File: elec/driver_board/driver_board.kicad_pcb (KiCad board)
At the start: 2 copper layers, 226.2 x 90.5 mm, 123 parts, among them J1 rotary_encoder, J10 Conn motor 0, J11 Conn motor 1, J12 Conn motor 0, J13 Conn motor 1, J14 Conn motor 0, J15 Conn motor 1, J16 Conn motor 0, J17 Conn motor 1, J18 Conn motor 0, J19 Conn motor 1, J2 DCF77 board, J20 Conn motor 0, J21 Conn motor 1, J22 Conn motor 0, J23 Conn motor 1, J24 Conn motor 0, J25 Conn motor 1, J26 Conn motor 0, J27 Conn motor 1, J3 RTC, J4 Conn motor 0, J5 Conn motor 1, J6 Conn motor 0, J7 Conn motor 1, J8 Conn motor 0, J9 Conn motor 1, U1 ESP32-C3-DEVKITM-1, U11 74HCT595, U13 74HCT595, U15 74HCT595, U17 74HCT595, U19 74HCT595, U2 TXB0102DCT, U21 74HCT595, U23 74HCT595, U25 74HCT595, U3 74HCT595, U5 74HCT595, U7 74HCT595, U9 74HCT595

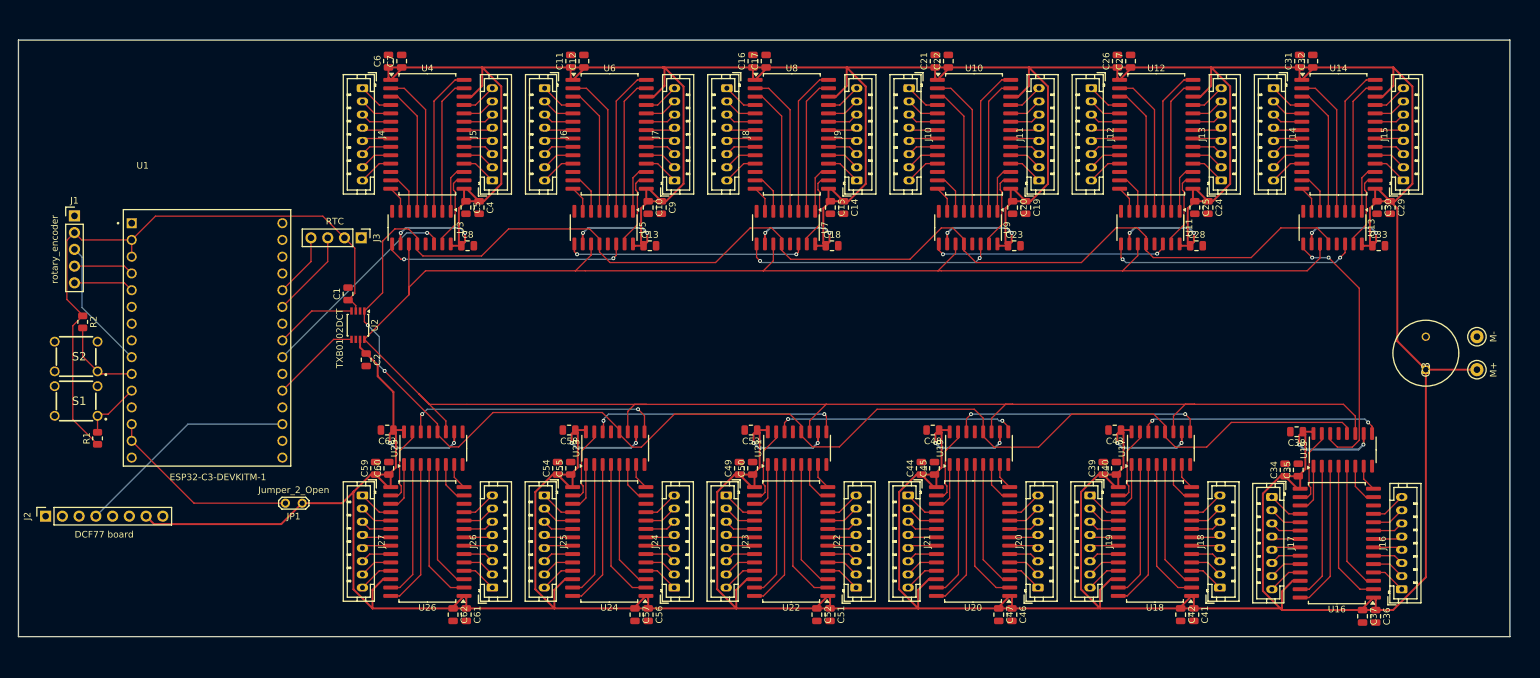
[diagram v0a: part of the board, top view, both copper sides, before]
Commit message: PCB done, ready to be ordered
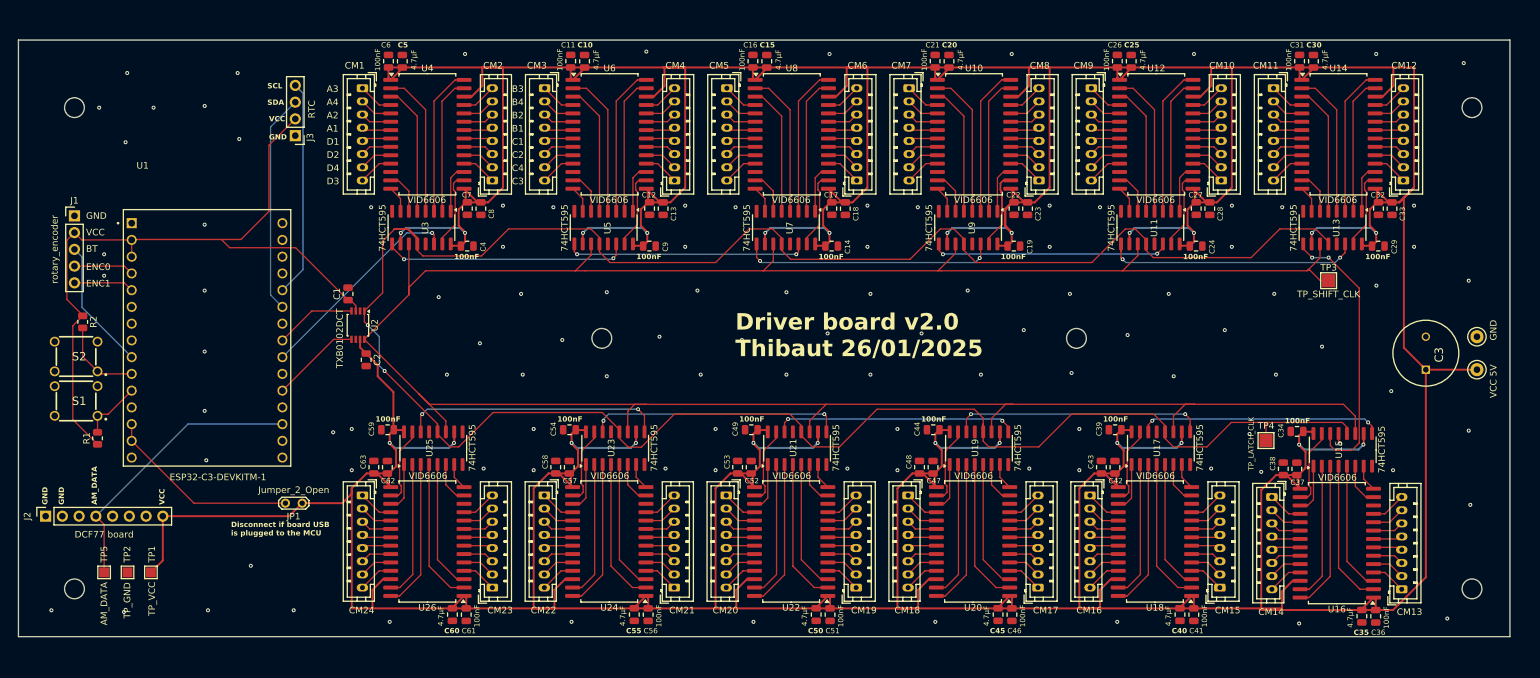
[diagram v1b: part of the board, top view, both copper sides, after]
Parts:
- added TP1: TP_VCC, TestPoint:TestPoint_Pad_1.5x1.5mm, F.Cu at (61.6, 120.5)
- added TP2: TP_GND, TestPoint:TestPoint_Pad_1.5x1.5mm, F.Cu at (58.0, 120.5)
- added TP3: TP_SHIFT_CLK, TestPoint:TestPoint_Pad_2.0x2.0mm, F.Cu at (240.2, 76.2)
- added TP4: TP_LATCH_CLK, TestPoint:TestPoint_Pad_2.0x2.0mm, F.Cu at (230.8, 100.5)
- added TP5: AM_DATA, TestPoint:TestPoint_Pad_1.5x1.5mm, F.Cu at (54.5, 120.5)
- GND_DCDC1: value M- -> GND
- U10, U12, U14, U16, U18, U20, U22, U24, U26, U4, U6, U8: value ~ -> VID6606
- VCC_DCDC1: value M+ -> VCC 5V
- moved C17 24.5 mm to (164.9, 65.3), turned to -90 degrees
- moved C22 24.5 mm to (192.5, 65.3), turned to -90 degrees
- moved C27 24.5 mm to (220.2, 65.3), turned to -90 degrees
- moved C32 24.5 mm to (247.8, 65.3), turned to -90 degrees
- moved C7 24.5 mm to (109.6, 65.3), turned to -90 degrees
- moved C12 24.5 mm to (137.2, 65.3), turned to -90 degrees
- moved C37 24.5 mm to (235.4, 104.8), turned to 90 degrees
- moved C42 24.5 mm to (207.8, 104.6), turned to 90 degrees
- moved C52 24.5 mm to (152.7, 104.6), turned to 90 degrees
- moved C62 24.5 mm to (97.5, 104.6), turned to 90 degrees
- moved C57 24.5 mm to (125.1, 104.6), turned to 90 degrees
- moved C47 24.5 mm to (180.2, 104.6), turned to 90 degrees
- moved C55 24.2 mm to (134.9, 126.9), turned to -90 degrees
- moved C35 24.2 mm to (245.3, 127.1), turned to -90 degrees
- moved C40 24.2 mm to (217.7, 126.9), turned to -90 degrees
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- renumbered J4 to CM1, J13 to CM10, J14 to CM11, J15 to CM12, J16 to CM13, J17 to CM14, J18 to CM15, J19 to CM16, J20 to CM17, J21 to CM18, J22 to CM19, J5 to CM2, J23 to CM20, J24 to CM21, J25 to CM22, J26 to CM23, J27 to CM24, J6 to CM3, J7 to CM4, J8 to CM5, J9 to CM6, J10 to CM7, J11 to CM8, J12 to CM9
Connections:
- J2 pad 7: VCC -> unconnected-(J2-Pin_7-Pad7)
- J2 pad 8: unconnected-(J2-Pin_8-Pad8) -> VCC
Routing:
- net VCC: track 1206.4 -> 1230.6 mm
- net /control_board/SCL_RTC: track 9.74 -> 32.8 mm
- net /control_board/SDA_RTC: track 13.3 -> 33.4 mm
- net /control_board/VCC_3V3: track 95.4 -> 111.1 mm
- net LATCH_CLOCK: track 371.0 -> 380.6 mm
- net /control_board/AM_DATA: track 34.1 -> 43.1 mm
- net /motor_driver3/DIR_D: track 11.9 -> 18.8 mm
- net /motor_driver3/DATA_OUT: track 37.2 -> 34.7 mm
- net GND: track 0.00 -> 1.65 mm, vias 0 -> 107
- net /motor_driver7/DATA_OUT: track 38.5 -> 39.6 mm
- net /motor_driver4/DATA_OUT: track 38.3 -> 39.5 mm
- net /motor_driver2/DATA_OUT: track 38.7 -> 39.8 mm
- net SHIFT_CLOCK: track 372.7 -> 373.6 mm
- net /motor_driver8/DATA_OUT: track 36.8 -> 36.0 mm
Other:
- outline, holes or cut-outs redrawn
- board text added: "A1"
- board text added: "A2"
- board text added: "A3"
- board text added: "A4"
- board text added: "AM_DATA"
- board text added: "B1"
- board text added: "B2"
- board text added: "B3"
- board text added: "B4"
- board text added: "BT"
- board text added: "C1"
- board text added: "C2"
- board text added: "C3"
- board text added: "C4"
- board text added: "D1"
- board text added: "D2"
- board text added: "D3"
- board text added: "D4"
- board text added: "Disconnect if board USB is plugged to the MCU"
- board text added: "Driver board v2.0 Thibaut 26/01/2025"
- board text added: "ENC0"
- board text added: "ENC1"
- board text added: "GND"
- board text added: "SCL"
- board text added: "SDA"
- board text added: "VCC"

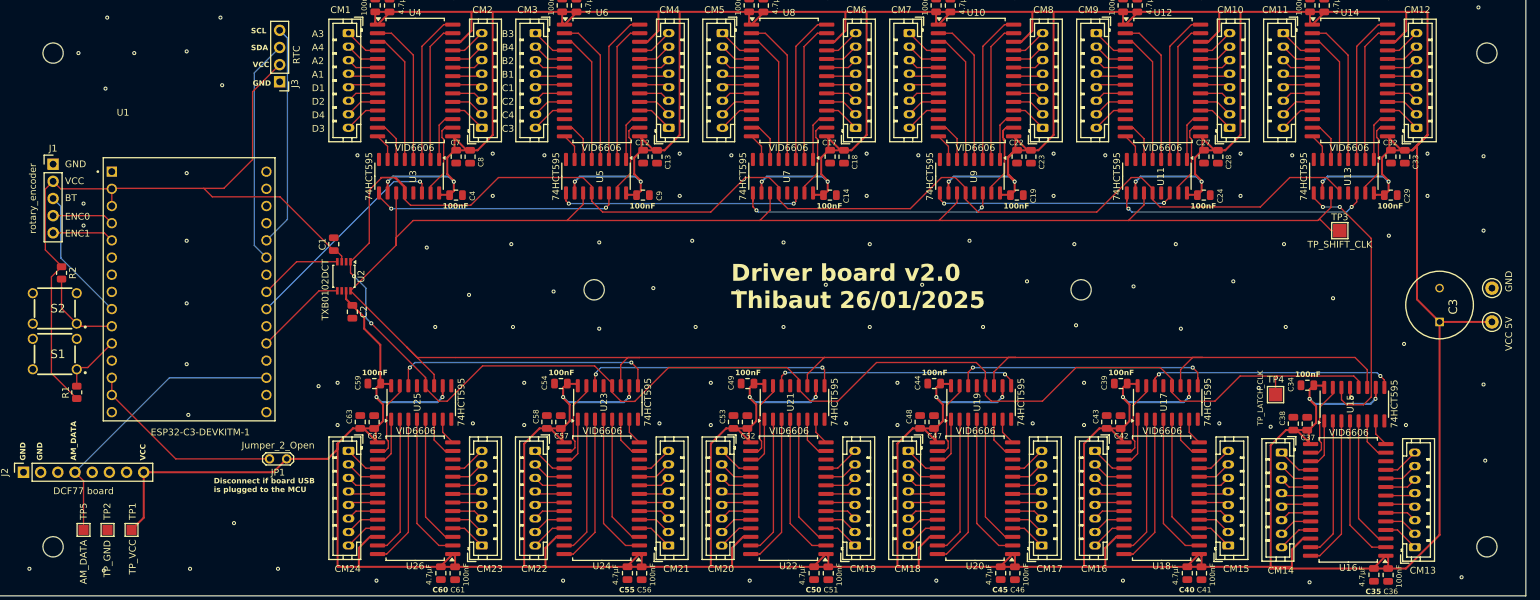
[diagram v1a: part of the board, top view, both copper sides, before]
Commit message: Update footprint of the level shifter
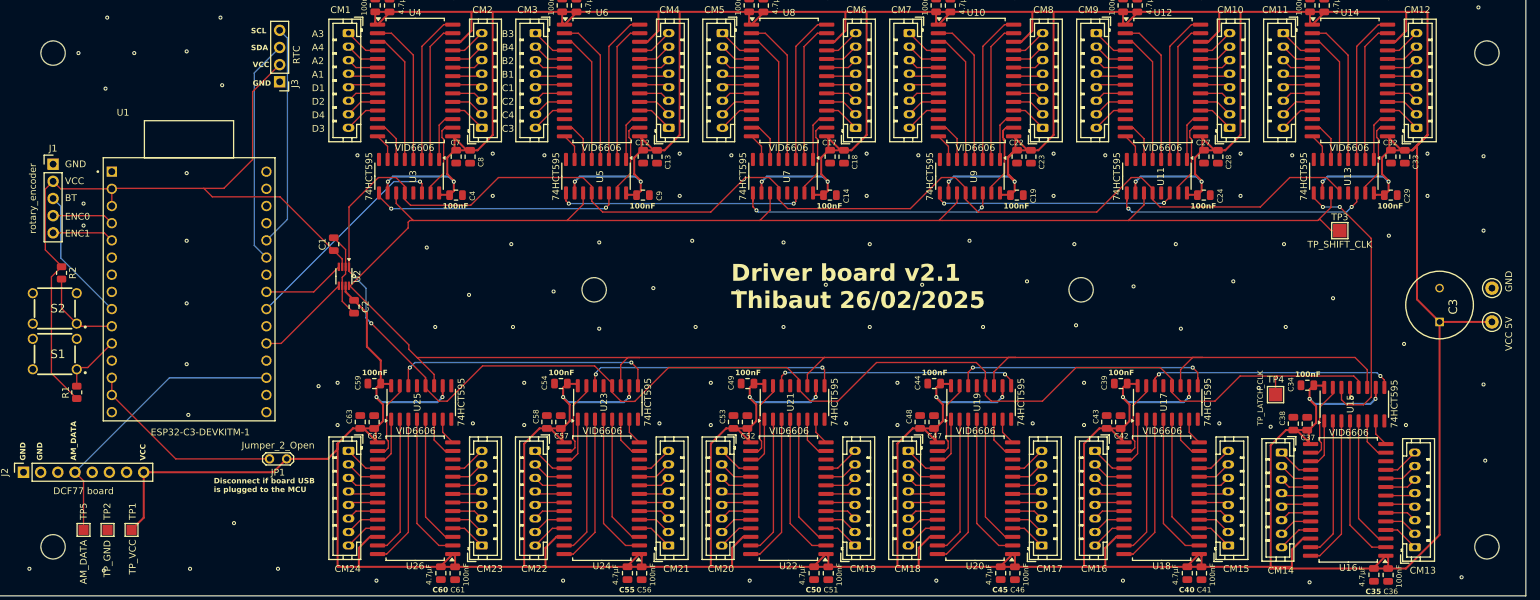
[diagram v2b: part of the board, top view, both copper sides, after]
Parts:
- U2: footprint Package_SO:TSSOP-8_3x3mm_P0.65mm -> Package_SO:VSSOP-8_2.3x2mm_P0.5mm
- moved C2 0.79 mm to (94.5, 87.5)
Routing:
- net GND: track 1.65 -> 14.5 mm
- net LATCH_CLOCK: track 380.6 -> 376.2 mm
- net SHIFT_CLOCK: track 373.6 -> 369.5 mm
- net VCC: track 1230.6 -> 1231.4 mm
- net /control_board/VCC_3V3: track 111.1 -> 111.7 mm
- net /control_board/SHIFT_CLOCK_3V3: track 13.7 -> 14.2 mm
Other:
- outline, holes or cut-outs redrawn
- board text added: "Driver board v2.1 Thibaut 26/02/2025"
- board text removed: "Driver board v2.0 Thibaut 26/01/2025"

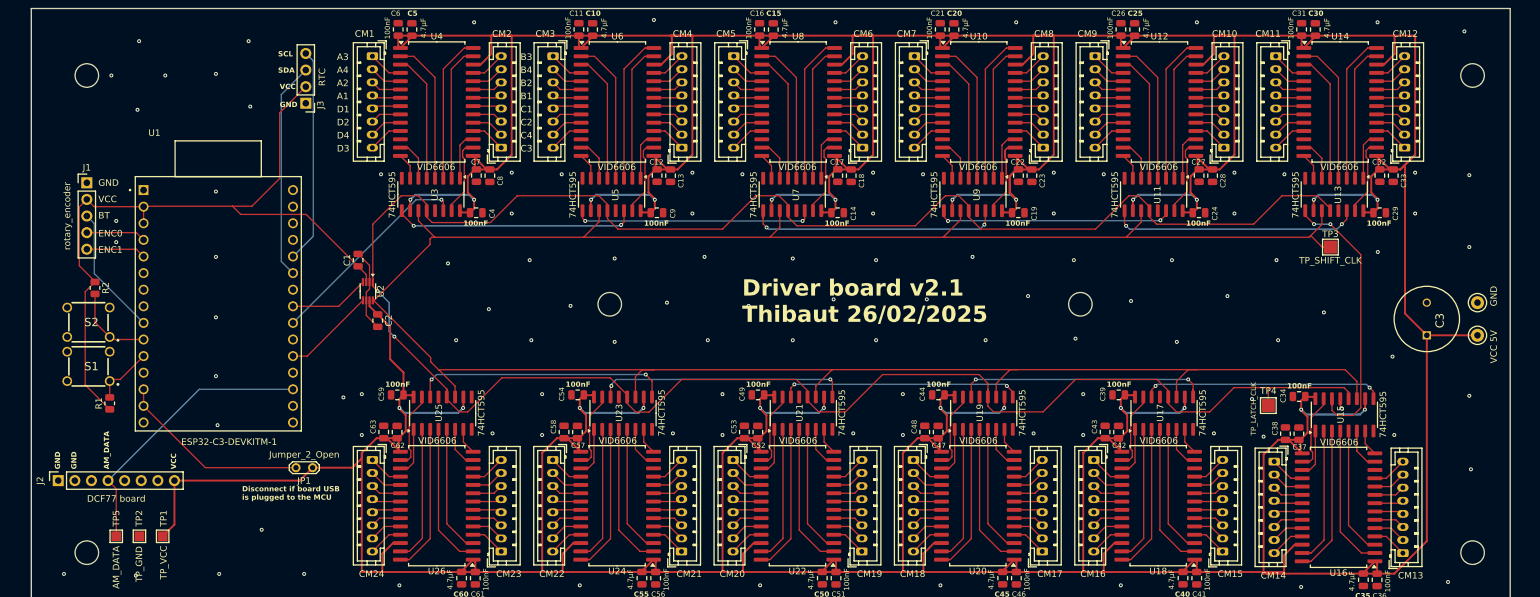
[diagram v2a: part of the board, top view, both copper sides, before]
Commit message: Various updates
Reposition rotary encoder
reposition RTC
add GND pads
update footprint of the big capa
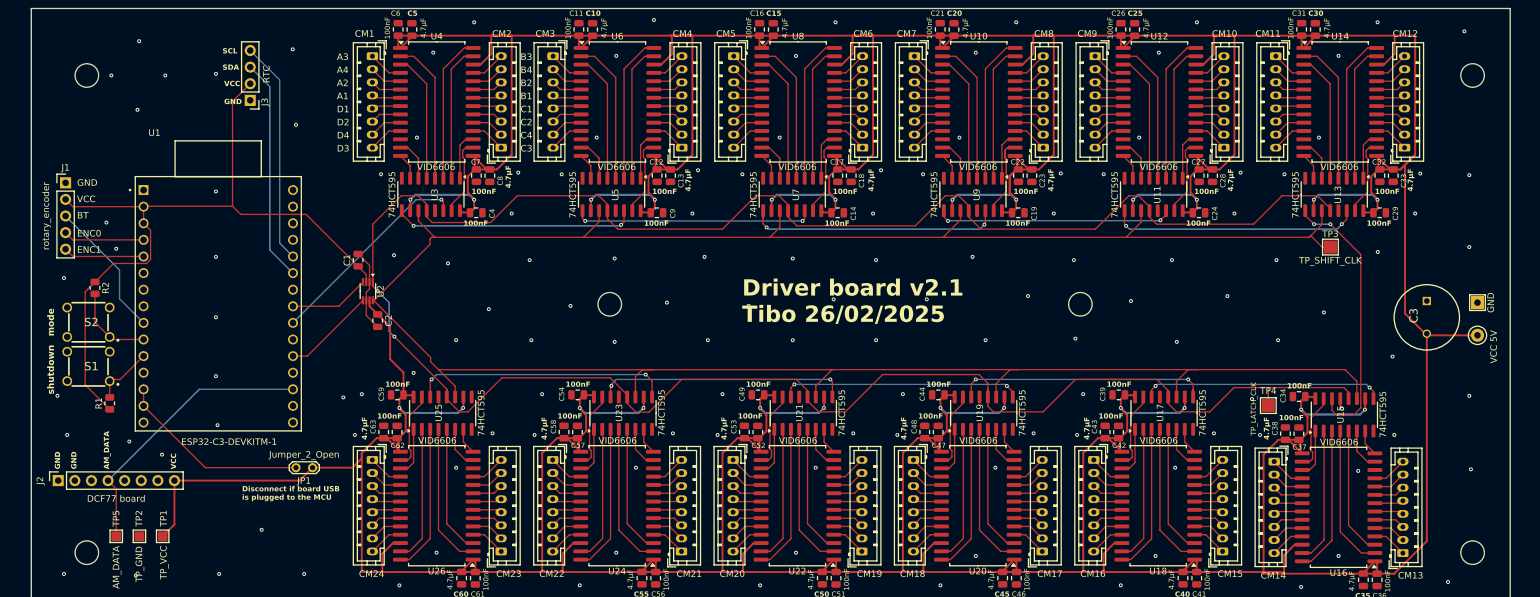
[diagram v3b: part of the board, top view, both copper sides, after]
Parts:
- GND_DCDC1: footprint TestPoint:TestPoint_Keystone_5000-5004_Miniature -> TestPoint:TestPoint_THTPad_2.0x2.0mm_Drill1.0mm
- S1: value Button shutdown -> shutdown
- S2: value Button mode -> mode
- moved J3 8.51 mm to (75.0, 53.8)
- moved C3 5.25 mm to (255.0, 84.5), turned to -90 degrees
- moved J1 3.25 mm to (46.8, 66.4)
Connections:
- C3 pad 1: VCC -> GND
- C3 pad 2: GND -> VCC
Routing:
- net /control_board/PIN_ENCODER_1: track 9.14 -> 12.4 mm
- net /control_board/PIN_ENCODER_0: track 9.14 -> 12.4 mm
- net /control_board/SCL_RTC: track 32.8 -> 34.2 mm
- net /control_board/PIN_BUTTON_ENCODER: track 19.9 -> 21.3 mm
- net /control_board/SDA_RTC: track 33.4 -> 34.2 mm
- net GND: vias 107 -> 138
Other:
- board text added: "Driver board v2.1 Tibo 26/02/2025"
- board text removed: "Driver board v2.1 Thibaut 26/02/2025"

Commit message: Update silkscreen
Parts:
- removed CM1, CM11, CM13, CM15, CM17, CM19, CM21, CM23, CM3, CM5, CM7, CM9: Conn motor 0, Connector_JST:JST_PH_B8B-PH-K_1x08_P2.00mm_Vertical
- removed CM10, CM12, CM14, CM16, CM18, CM2, CM20, CM22, CM24, CM4, CM6, CM8: Conn motor 1, Connector_JST:JST_PH_B8B-PH-K_1x08_P2.00mm_Vertical
- added M1: Conn motor 0, Connector_JST:JST_PH_B8B-PH-K_1x08_P2.00mm_Vertical, F.Cu at (93.7, 47.0)
- added M10: Conn motor 1, Connector_JST:JST_PH_B8B-PH-K_1x08_P2.00mm_Vertical, F.Cu at (224.0, 61.0)
- added M11: Conn motor 0, Connector_JST:JST_PH_B8B-PH-K_1x08_P2.00mm_Vertical, F.Cu at (231.9, 47.0)
- added M12: Conn motor 1, Connector_JST:JST_PH_B8B-PH-K_1x08_P2.00mm_Vertical, F.Cu at (251.6, 61.0)
- added M13: Conn motor 0, Connector_JST:JST_PH_B8B-PH-K_1x08_P2.00mm_Vertical, F.Cu at (251.3, 123.1)
- added M14: Conn motor 1, Connector_JST:JST_PH_B8B-PH-K_1x08_P2.00mm_Vertical, F.Cu at (231.6, 109.1)
- added M15: Conn motor 0, Connector_JST:JST_PH_B8B-PH-K_1x08_P2.00mm_Vertical, F.Cu at (223.8, 122.8)
- added M16: Conn motor 1, Connector_JST:JST_PH_B8B-PH-K_1x08_P2.00mm_Vertical, F.Cu at (204.1, 108.8)
- added M17: Conn motor 0, Connector_JST:JST_PH_B8B-PH-K_1x08_P2.00mm_Vertical, F.Cu at (196.2, 122.8)
- added M18: Conn motor 1, Connector_JST:JST_PH_B8B-PH-K_1x08_P2.00mm_Vertical, F.Cu at (176.5, 108.8)
- added M19: Conn motor 0, Connector_JST:JST_PH_B8B-PH-K_1x08_P2.00mm_Vertical, F.Cu at (168.6, 122.8)
- added M2: Conn motor 1, Connector_JST:JST_PH_B8B-PH-K_1x08_P2.00mm_Vertical, F.Cu at (113.4, 61.0)
- added M20: Conn motor 1, Connector_JST:JST_PH_B8B-PH-K_1x08_P2.00mm_Vertical, F.Cu at (148.9, 108.8)
- added M21: Conn motor 0, Connector_JST:JST_PH_B8B-PH-K_1x08_P2.00mm_Vertical, F.Cu at (141.0, 122.8)
- added M22: Conn motor 1, Connector_JST:JST_PH_B8B-PH-K_1x08_P2.00mm_Vertical, F.Cu at (121.3, 108.8)
- added M23: Conn motor 0, Connector_JST:JST_PH_B8B-PH-K_1x08_P2.00mm_Vertical, F.Cu at (113.4, 122.8)
- added M24: Conn motor 1, Connector_JST:JST_PH_B8B-PH-K_1x08_P2.00mm_Vertical, F.Cu at (93.7, 108.8)
- added M3: Conn motor 0, Connector_JST:JST_PH_B8B-PH-K_1x08_P2.00mm_Vertical, F.Cu at (121.3, 47.0)
- added M4: Conn motor 1, Connector_JST:JST_PH_B8B-PH-K_1x08_P2.00mm_Vertical, F.Cu at (141.0, 61.0)
- added M5: Conn motor 0, Connector_JST:JST_PH_B8B-PH-K_1x08_P2.00mm_Vertical, F.Cu at (149.0, 47.0)
- added M6: Conn motor 1, Connector_JST:JST_PH_B8B-PH-K_1x08_P2.00mm_Vertical, F.Cu at (168.7, 61.0)
- added M7: Conn motor 0, Connector_JST:JST_PH_B8B-PH-K_1x08_P2.00mm_Vertical, F.Cu at (176.6, 47.0)
- added M8: Conn motor 1, Connector_JST:JST_PH_B8B-PH-K_1x08_P2.00mm_Vertical, F.Cu at (196.3, 61.0)
- added M9: Conn motor 0, Connector_JST:JST_PH_B8B-PH-K_1x08_P2.00mm_Vertical, F.Cu at (204.3, 47.0)
- S1: value shutdown -> Button shutdown
- S2: value mode -> Button mode
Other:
- board text added: "DATA_OUT"
- board text added: "Disconnect if USB is plugged to the ESP32"
- board text added: "Driver board v2.1 Thibaut 26/02/2025"
- board text added: "LATCH"
- board text added: "SCL_RTC"
- board text added: "SDA_RTC"
- board text added: "SHIFT_CLK"
- board text removed: "Disconnect if board USB is plugged to the MCU"
- board text removed: "Driver board v2.1 Tibo 26/02/2025"

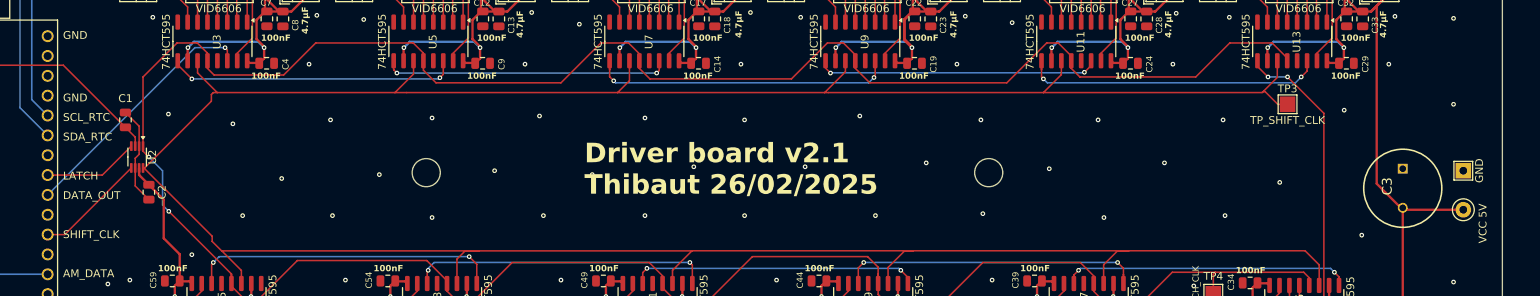
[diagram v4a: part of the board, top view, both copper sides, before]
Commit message: Update symbols
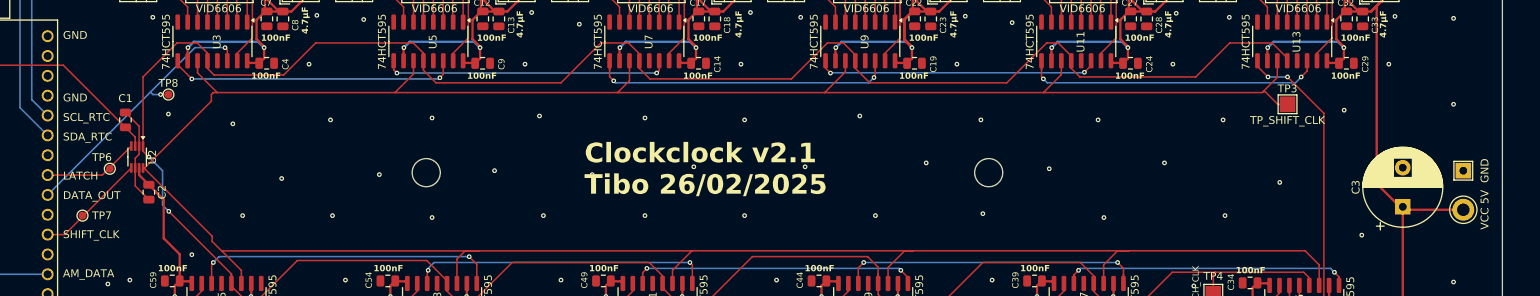
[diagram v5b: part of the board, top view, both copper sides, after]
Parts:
- added TP6: TP_LATCH_CLK, TestPoint:TestPoint_Pad_D1.0mm, F.Cu at (89.5, 84.5)
- added TP7: TP_SHIFT_CLK, TestPoint:TestPoint_Pad_D1.0mm, F.Cu at (86.0, 90.5)
- added TP8: DATA_OUT, TestPoint:TestPoint_Pad_D1.0mm, F.Cu at (97.0, 75.0)
- C3: footprint Samacsys:CAPPRD500W65D1000H2200 -> Capacitor_THT:CP_Radial_D10.0mm_P5.00mm
- VCC_DCDC1: footprint TestPoint:TestPoint_Keystone_5000-5004_Miniature -> TestPoint:TestPoint_Keystone_5005-5009_Compact
- moved C3 4.87 mm to (255.0, 89.4), turned to 90 degrees
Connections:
- C3 pad 1: GND -> VCC
- C3 pad 2: VCC -> GND
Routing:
- net /control_board/DATA_OUT: track 32.3 -> 34.7 mm, vias 1 -> 2
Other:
- board text added: "Clockclock v2.1 Tibo 26/02/2025"
- board text removed: "Driver board v2.1 Thibaut 26/02/2025"
